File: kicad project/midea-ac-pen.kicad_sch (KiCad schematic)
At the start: 9 parts, among them J1 Conn_01x08_Pin, J2 Conn_01x08_Pin, J3 USB_A, Q1 2N3904, Q2 2N3904

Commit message: draw pcb
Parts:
- removed J1, J2: Conn_01x08_Pin, symbol Connector:Conn_01x08_Pin
- removed J3: USB_A, symbol Connector:USB_A
- added J1: Conn_01x04_Pin, ESP32_C3_Super_Mini:PCB_USB, symbol Connector:Conn_01x04_Pin
- added U1: ~, ESP32_C3_Super_Mini:ESP32_C3_Super_Mini, symbol ESP32_C3_Super_Mini:ESP32_C3_Super_Mini
- Q1: renamed from Q2; footprint (none) -> Package_TO_SOT_THT:TO-92
- Q2: renamed from Q1; footprint (none) -> Package_TO_SOT_THT:TO-92
- R1: renamed from R3; value R -> 10k; footprint (none) -> Resistor_THT:R_Axial_DIN0204_L3.6mm_D1.6mm_P2.54mm_Vertical
- R2, R4: value R -> 10k; footprint (none) -> Resistor_THT:R_Axial_DIN0204_L3.6mm_D1.6mm_P2.54mm_Vertical
- R3: renamed from R1; value R -> 10k; footprint (none) -> Resistor_THT:R_Axial_DIN0204_L3.6mm_D1.6mm_P2.54mm_Vertical
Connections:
- net 3.3V: now also U1.5 (3V3)
- net 5V: now also R3.2, J1.1 (Pin_1), U1.7 (5V); no longer R3.1
- net AC_RX: now also R3.1, J1.2 (Pin_2); no longer R3.2
- net AC_TX: now also J1.3 (Pin_3)
- net ESP_RX: now also U1.3 (GPIO_3)
- net ESP_TX: now also R2.2, U1.1 (GPIO_1); no longer R2.1
- net GND: now also J1.4 (Pin_4), U1.6 (G)
- net at Q2.2 (B): now also R2.1; no longer R2.2
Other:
- note removed: "Fix this lol"
- moved on the sheet: Q1, Q2, R1, R2, R3, R4

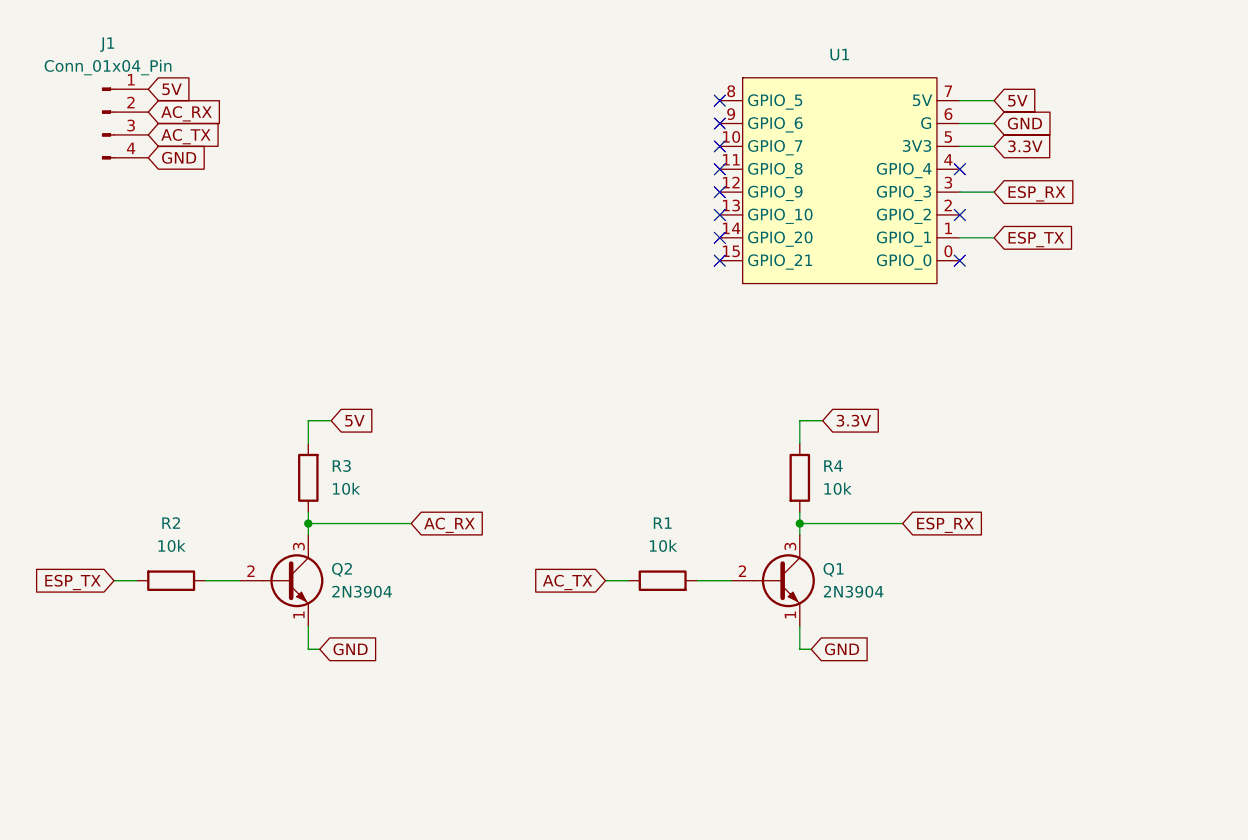
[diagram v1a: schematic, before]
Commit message: Fix library names and remove value field from ESP32 symbol
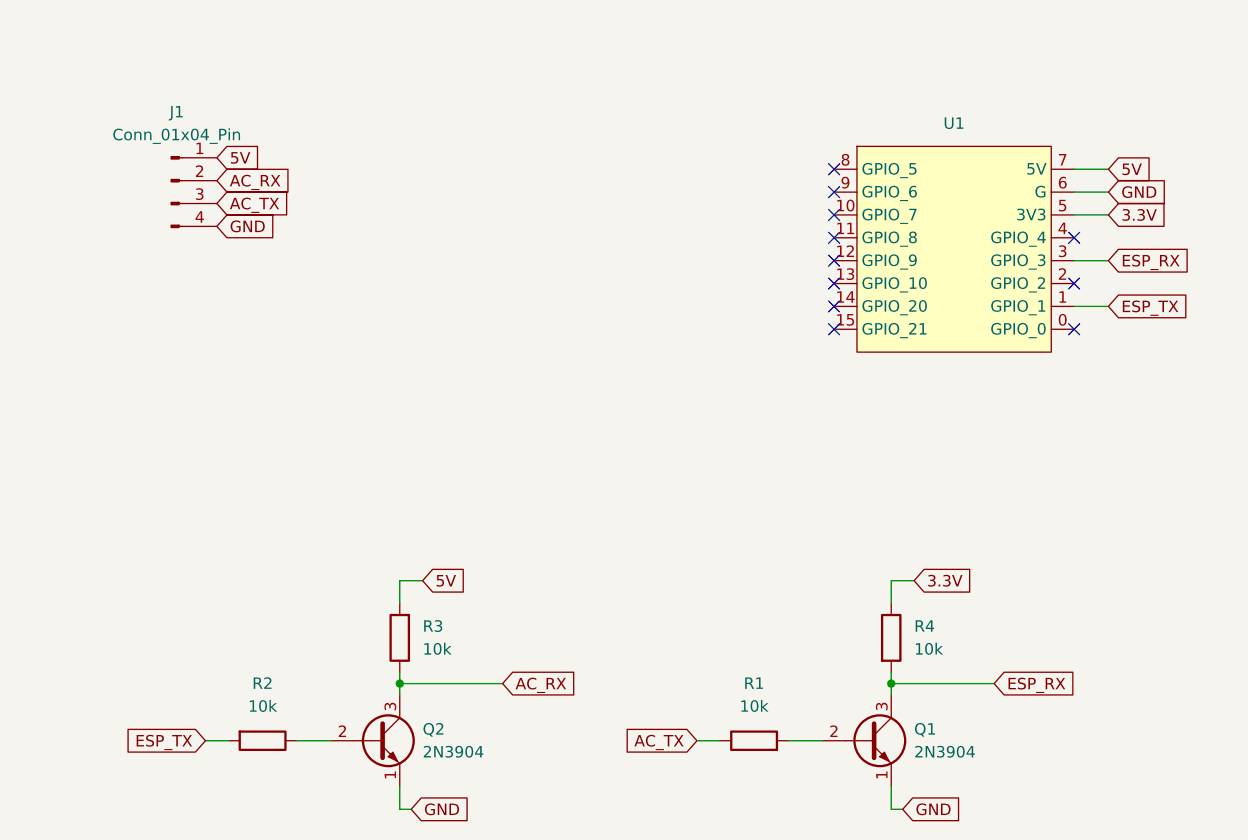
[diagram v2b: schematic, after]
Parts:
- J1: footprint ESP32_C3_Super_Mini:PCB_USB -> Project Libraries:PCB_USB
- U1: value ~ -> (none); footprint ESP32_C3_Super_Mini:ESP32_C3_Super_Mini -> Project Libraries:ESP32_C3_Super_Mini; symbol ESP32_C3_Super_Mini:ESP32_C3_Super_Mini -> Project Symbols:ESP32_C3_Super_Mini
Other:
- moved on the sheet: J1, Q1, Q2, R1, R2, R3, R4, U1

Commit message: Finish board design
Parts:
- added JP1, JP3: SolderJumper_2_Open, Jumper:SolderJumper-2_P1.3mm_Open_RoundedPad1.0x1.5mm, symbol Jumper:SolderJumper_2_Open
- added JP2, JP4: SolderJumper_2_Bridged, Jumper:SolderJumper-2_P1.3mm_Bridged_RoundedPad1.0x1.5mm, symbol Jumper:SolderJumper_2_Bridged
- U1: value (none) -> ~
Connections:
- net AC_RX: now also JP2.2 (B), JP3.1 (A); no longer J1.2 (Pin_2)
- net AC_TX: now also JP1.1 (A), JP4.2 (B); no longer J1.3 (Pin_3)
- new net D+: J1.3 (Pin_3), JP1.2 (B), JP2.1 (A)
- new net D-: J1.2 (Pin_2), JP3.2 (B), JP4.1 (A)
